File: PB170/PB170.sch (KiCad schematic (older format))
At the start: 33 parts, among them J1 USB_C_Receptacle_USB2.0-Conne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, J2 USB_B_Micro, Q1 P-MOSFET-MLP_HS, Q2 BC817, SW1 SW_MEC_5E, SW2 SW_MEC_5E

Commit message: 10-02-Martin
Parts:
- added C?: 10n, Capacitor_SMD:C_0402_1005Metric, symbol Device:C
- added C?: 47u, Capacitor_SMD:C_0805_2012Metric, symbol Device:C
- added R? (x2): 10k, Resistor_SMD:R_0402_1005Metric, symbol Device:R
- added U? (x5): 74HC74, Package_SO:TSSOP-14_4.4x5mm_P0.65mm, symbol 74xx:74HC74
- added U?: NE555DR, Package_SO:SOIC-8_3.9x4.9mm_P1.27mm, symbol Timer:NE555D
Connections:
- net +5V: now also R?.1, U?.4 (R), U?.8 (VCC)
- net GND: now also C?.2, C?.2, U?.1 (GND), U?.6 (~Q), U?.6 (~Q), U?.6 (~Q), U?.6 (~Q), U?.6 (~Q)
- new net: C?.1, R?.2, U?.2 (TR), U?.6 (THR)
- new net: C?.1, U?.5 (CV)
- new net: R?.1, R?.2, U?.7 (DIS)
- new net Q0: U?.5 (Q)
- new net Q1: U?.5 (Q)
- new net Q2: U?.5 (Q)
- new net Q3: U?.5 (Q)
- new net Q4: U?.5 (Q)

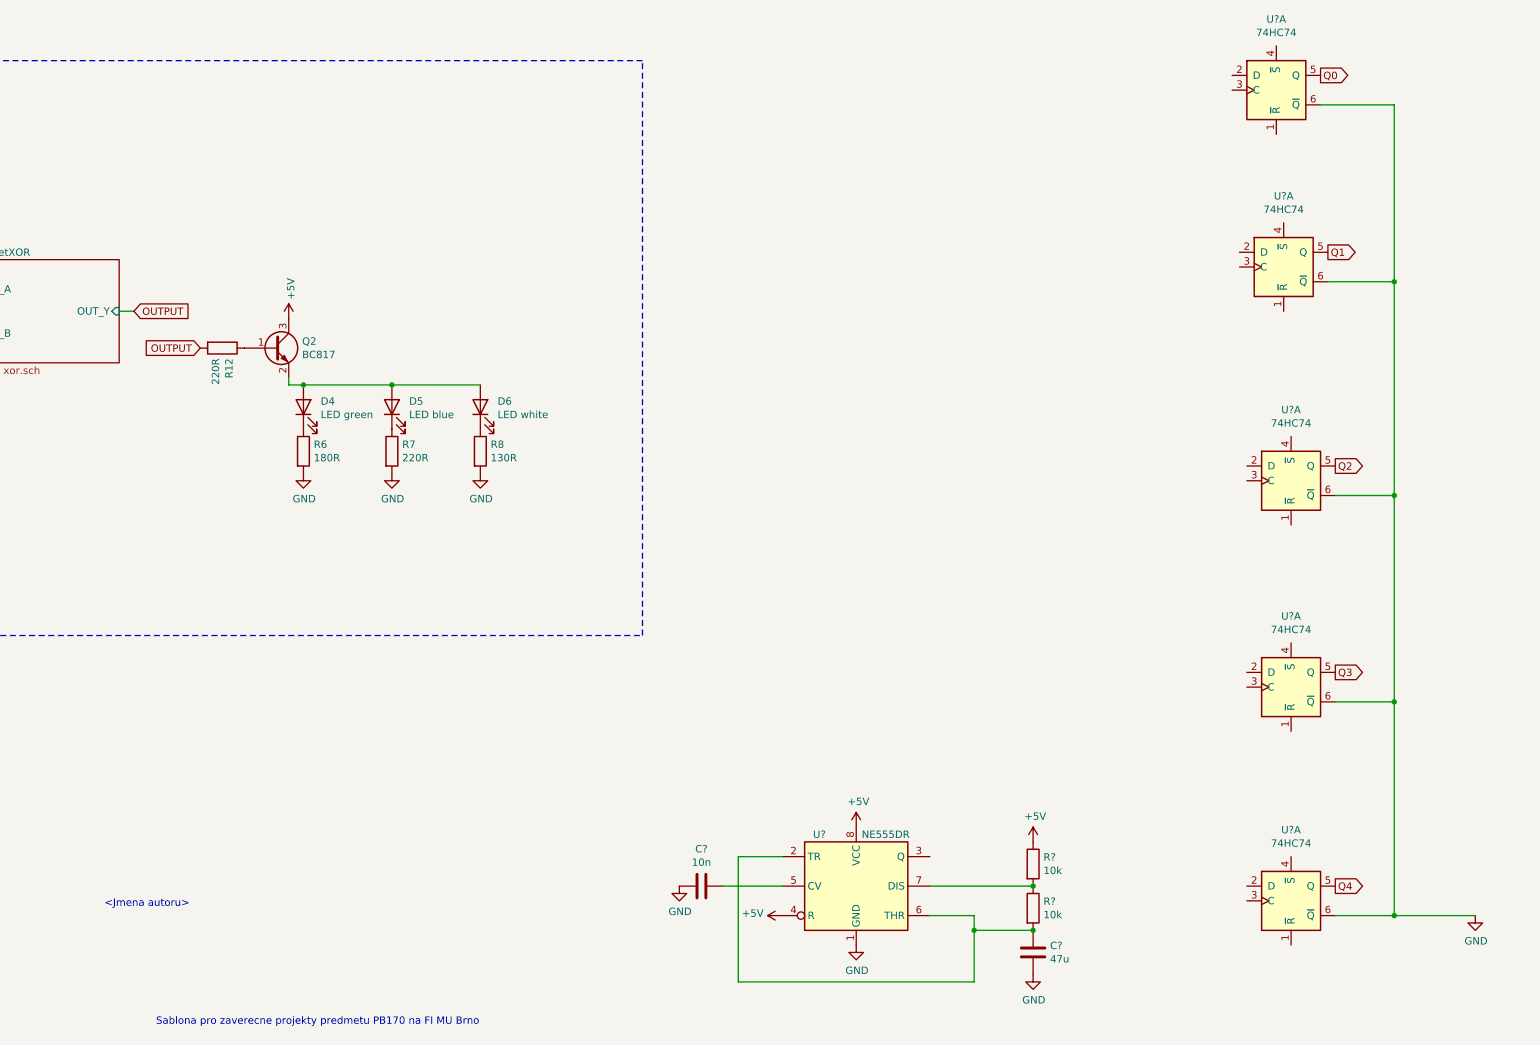
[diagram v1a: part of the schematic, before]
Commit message: Flip-Flops changed
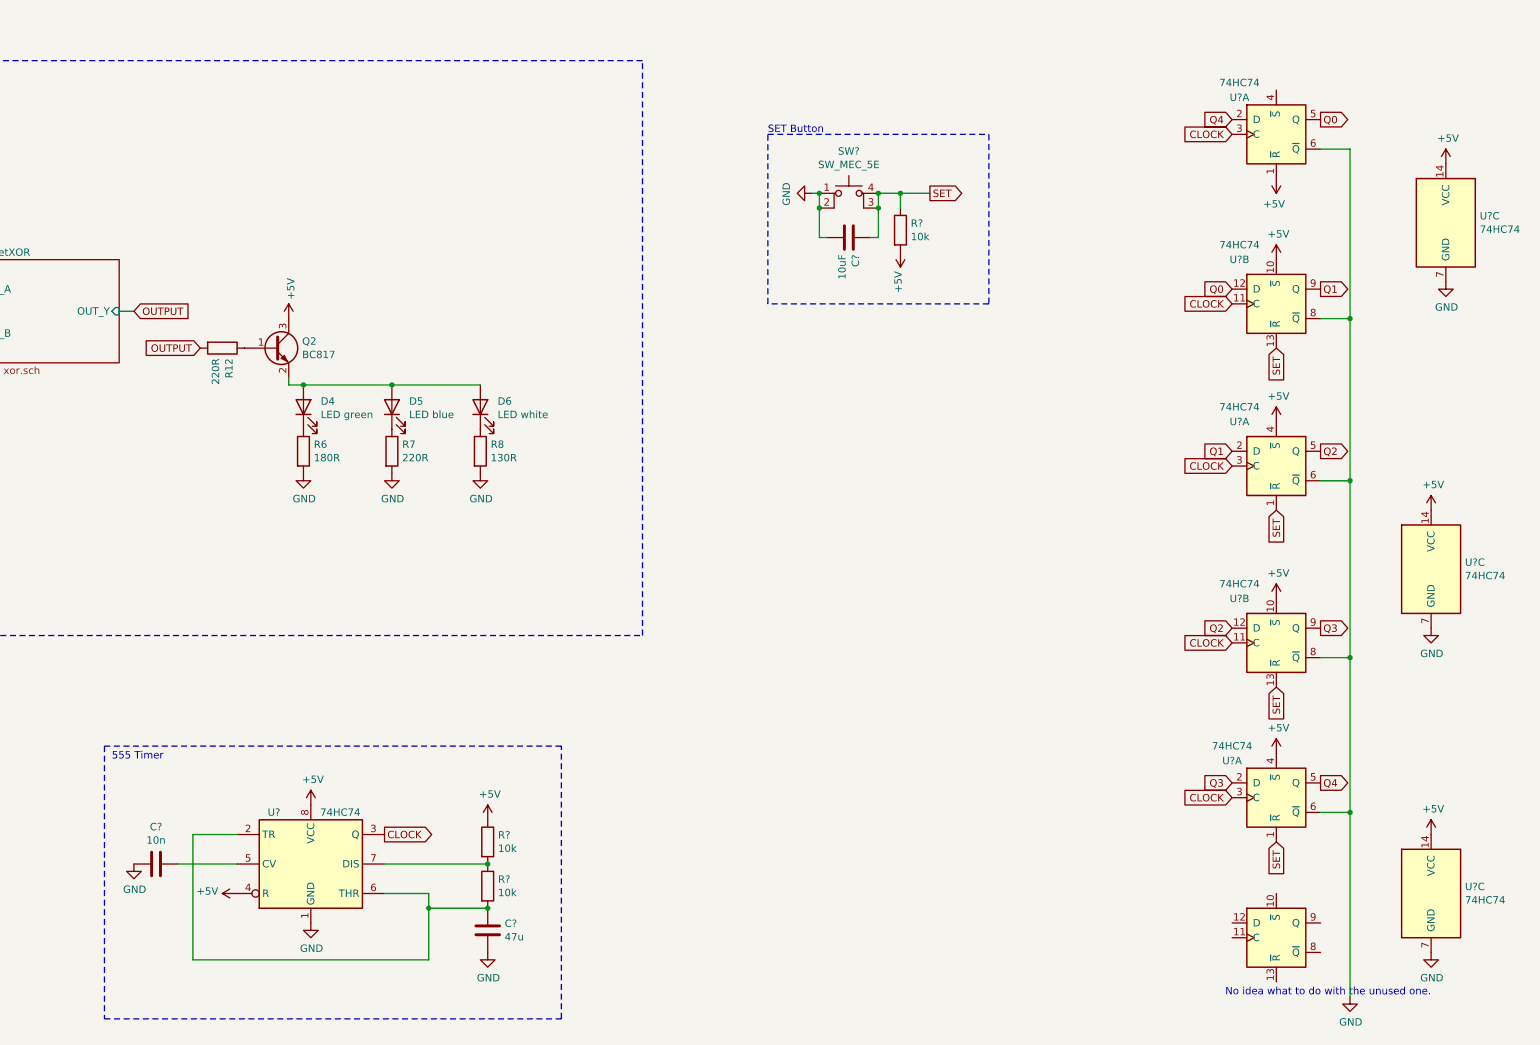
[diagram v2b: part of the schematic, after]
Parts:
- removed U? (x4): 74HC74, Package_SO:TSSOP-14_4.4x5mm_P0.65mm, symbol 74xx:74HC74
- added C?: 10uF, Capacitors_SMD:C_0805, symbol Device:C
- added R?: 10k, Resistors_SMD:R_0603, symbol Device:R
- added SW?: SW_MEC_5E, PB170:TactileSwitch_C381064, symbol Switch:SW_MEC_5E
- added U? (x8): 74HC74, Package_SO:TSSOP-14_4.4x5mm_P0.65mm, symbol 74xx:74HC74
- U?: value NE555DR -> 74HC74; footprint Package_SO:SOIC-8_3.9x4.9mm_P1.27mm -> Package_SO:TSSOP-14_4.4x5mm_P0.65mm
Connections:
- net +5V: now also U?.1 (~R), R?.2, U?.10 (~S), U?.10 (~S), U?.14 (VCC), U?.14 (VCC), U?.14 (VCC), U?.4 (~S), U?.4 (~S)
- net GND: now also C?.2, SW?.1, SW?.2, U?.6 (~Q), U?.6 (~Q), U?.7 (GND), U?.7 (GND), U?.7 (GND), U?.8 (~Q), U?.8 (~Q)
- net Q0: now also U?.12 (D)
- net Q1: now also U?.2 (D), U?.9 (Q)
- net Q2: now also U?.12 (D), U?.5 (Q)
- net Q3: now also U?.2 (D), U?.9 (Q)
- net Q4: now also U?.2 (D), U?.5 (Q)
- net CLOCK: now reaches U?.3 (C)
- net CLOCK: now also U?.3 (Q), U?.11 (C), U?.11 (C), U?.3 (C), U?.3 (C)
- new net SET: C?.1, R?.1, SW?.3 (K), SW?.4 (A), U?.1 (~R), U?.1 (~R), U?.13 (~R), U?.13 (~R)
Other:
- note added: "555 Timer"
- note added: "No idea what to do with the unused one."
- note added: "SET Button"
- note removed: "<Jmena autoru>"
- note removed: "Sablona pro zaverecne projekty predmetu PB170 na FI MU Brno"
- moved on the sheet: C?, R?, U?, U?A
